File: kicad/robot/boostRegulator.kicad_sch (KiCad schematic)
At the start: 22 parts, among them U5 LSF0102DCTR, U6 MAX77857

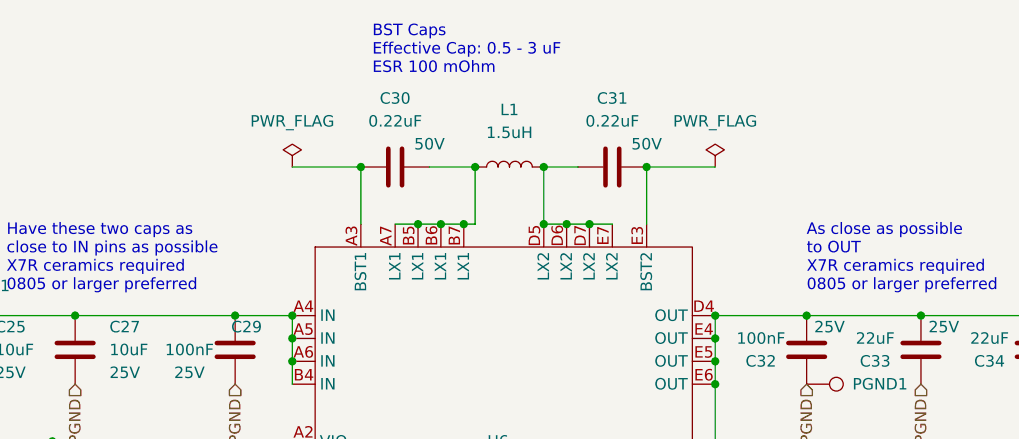
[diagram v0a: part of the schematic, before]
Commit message: Added power flags to Max77857 LX{1,2} pins
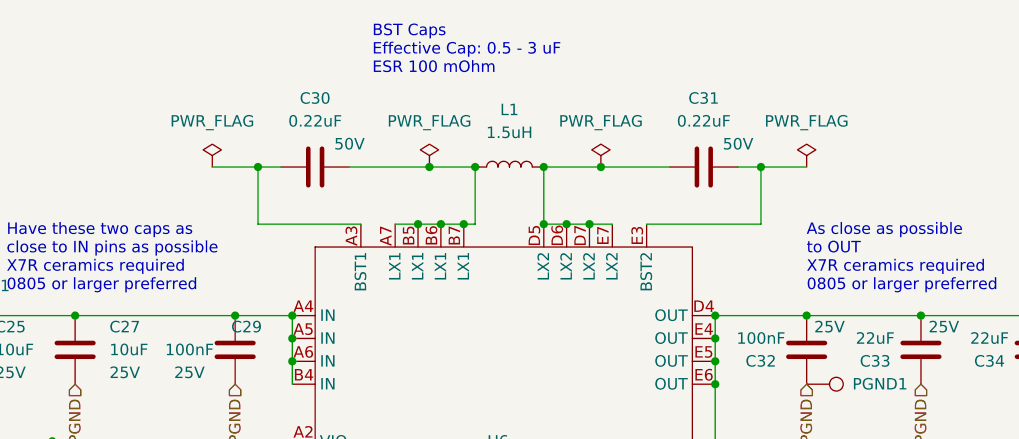
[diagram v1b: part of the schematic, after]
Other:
- moved on the sheet: C30, C31
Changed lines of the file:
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@@
   (junction (at 187.96 80.01) (diameter 0) (color 0 0 0 0)
   )
-  (junction (at 210.82 73.66) (diameter 0) (color 0 0 0 0)
-  )
   (junction (at 189.23 140.97) (diameter 0) (color 0 0 0 0)
   )
@@
   (junction (at 199.39 80.01) (diameter 0) (color 0 0 0 0)
   )
+  (junction (at 205.74 73.66) (diameter 0) (color 0 0 0 0)
+  )
   (junction (at 185.42 80.01) (diameter 0) (color 0 0 0 0)
   )
@@
   (junction (at 118.11 104.14) (diameter 0) (color 0 0 0 0)
   )
+  (junction (at 186.69 73.66) (diameter 0) (color 0 0 0 0)
+  )
   (junction (at 199.39 73.66) (diameter 0) (color 0 0 0 0)
   )
@@
   (junction (at 194.31 140.97) (diameter 0) (color 0 0 0 0)
   )
+  (junction (at 167.64 73.66) (diameter 0) (color 0 0 0 0)
+  )
   (junction (at 228.6 90.17) (diameter 0) (color 0 0 0 0)
   )
-  (junction (at 179.07 73.66) (diameter 0) (color 0 0 0 0)
-  )
   (junction (at 204.47 80.01) (diameter 0) (color 0 0 0 0)
   )
@@
   )
   (junction (at 109.22 129.54) (diameter 0) (color 0 0 0 0)
+  )
+  (junction (at 223.52 73.66) (diameter 0) (color 0 0 0 0)
   )
   (no_connect (at 171.45 121.92))
@@
     (stroke (width 0) (type default) (color 0 0 0 0))
   )
-  (wire (pts (xy 179.07 73.66) (xy 179.07 80.01))
-    (stroke (width 0) (type default) (color 0 0 0 0))
-  )
   (wire (pts (xy 109.22 119.38) (xy 109.22 129.54))
     (stroke (width 0) (type default) (color 0 0 0 0))
@@
     (stroke (width 0) (type default) (color 0 0 0 0))
   )
-  (wire (pts (xy 210.82 73.66) (xy 218.44 73.66))
+  (wire (pts (xy 220.98 73.66) (xy 223.52 73.66))
     (stroke (width 0) (type default) (color 0 0 0 0))
   )
@@
     (stroke (width 0) (type default) (color 0 0 0 0))
   )
+  (wire (pts (xy 210.82 80.01) (xy 223.52 80.01))
+    (stroke (width 0) (type default) (color 0 0 0 0))
+  )
   (wire (pts (xy 194.31 140.97) (xy 196.85 140.97))
     (stroke (width 0) (type default) (color 0 0 0 0))
@@
     (stroke (width 0) (type default) (color 0 0 0 0))
   )
+  (wire (pts (xy 186.69 73.66) (xy 191.77 73.66))
+    (stroke (width 0) (type default) (color 0 0 0 0))
+  )
   (wire (pts (xy 109.22 104.14) (xy 118.11 104.14))
     (stroke (width 0) (type default) (color 0 0 0 0))
@@
     (stroke (width 0) (type default) (color 0 0 0 0))
   )
-  (wire (pts (xy 199.39 73.66) (xy 203.2 73.66))
+  (wire (pts (xy 199.39 73.66) (xy 205.74 73.66))
     (stroke (width 0) (type default) (color 0 0 0 0))
   )
@@
     (stroke (width 0) (type default) (color 0 0 0 0))
   )
+  (wire (pts (xy 223.52 80.01) (xy 223.52 73.66))
+    (stroke (width 0) (type default) (color 0 0 0 0))
+  )
   (wire (pts (xy 109.22 111.76) (xy 109.22 104.14))
     (stroke (width 0) (type default) (color 0 0 0 0))
   )
+  (wire (pts (xy 167.64 80.01) (xy 167.64 73.66))
+    (stroke (width 0) (type default) (color 0 0 0 0))
+  )
   (wire (pts (xy 109.22 129.54) (xy 171.45 129.54))
     (stroke (width 0) (type default) (color 0 0 0 0))
@@
     (stroke (width 0) (type default) (color 0 0 0 0))
   )
-  (wire (pts (xy 186.69 73.66) (xy 191.77 73.66))
-    (stroke (width 0) (type default) (color 0 0 0 0))
-  )
-  (wire (pts (xy 210.82 73.66) (xy 210.82 80.01))
+  (wire (pts (xy 177.8 73.66) (xy 186.69 73.66))
     (stroke (width 0) (type default) (color 0 0 0 0))
   )
@@
     (stroke (width 0) (type default) (color 0 0 0 0))
   )
+  (wire (pts (xy 205.74 73.66) (xy 213.36 73.66))
+    (stroke (width 0) (type default) (color 0 0 0 0))
+  )
   (wire (pts (xy 57.15 116.84) (xy 60.96 116.84))
     (stroke (width 0) (type default) (color 0 0 0 0))
@@
     (stroke (width 0) (type default) (color 0 0 0 0))
   )
+  (wire (pts (xy 223.52 73.66) (xy 228.6 73.66))
+    (stroke (width 0) (type default) (color 0 0 0 0))
+  )
   (wire (pts (xy 254 90.17) (xy 259.08 90.17))
     (stroke (width 0) (type default) (color 0 0 0 0))
@@
     (stroke (width 0) (type default) (color 0 0 0 0))
   )
-  (wire (pts (xy 171.45 73.66) (xy 179.07 73.66))
+  (wire (pts (xy 167.64 73.66) (xy 170.18 73.66))
+    (stroke (width 0) (type default) (color 0 0 0 0))
+  )
+  (wire (pts (xy 162.56 73.66) (xy 167.64 73.66))
     (stroke (width 0) (type default) (color 0 0 0 0))
   )
   (wire (pts (xy 118.11 111.76) (xy 118.11 104.14))
+    (stroke (width 0) (type default) (color 0 0 0 0))
+  )
+  (wire (pts (xy 179.07 80.01) (xy 167.64 80.01))
     (stroke (width 0) (type default) (color 0 0 0 0))
   )
@@
     (effects (font (size 1.27 1.27)) (justify right))
   )
-  (symbol (lib_id "power:PWR_FLAG") (at 218.44 73.66 0) (unit 1)
-    (in_bom yes) (on_board yes) (fields_autoplaced)
-    (property "Reference" "#FLG0104" (id 0) (at 218.44 71.755 0)
-      (effects (font (size 1.27 1.27)) hide)
-    )
-    (property "Value" "PWR_FLAG" (id 1) (at 218.44 68.58 0))
-    (property "Footprint" "" (id 2) (at 218.44 73.66 0)
-      (effects (font (size 1.27 1.27)) hide)
-    )
-    (property "Datasheet" "~" (id 3) (at 218.44 73.66 0)
+  (symbol (lib_id "power:PWR_FLAG") (at 228.6 73.66 0) (unit 1)
+    (in_bom yes) (on_board yes) (fields_autoplaced)
+    (property "Reference" "#FLG0104" (id 0) (at 228.6 71.755 0)
+      (effects (font (size 1.27 1.27)) hide)
+    )
+    (property "Value" "PWR_FLAG" (id 1) (at 228.6 68.58 0))
+    (property "Footprint" "" (id 2) (at 228.6 73.66 0)
+      (effects (font (size 1.27 1.27)) hide)
+    )
+    (property "Datasheet" "~" (id 3) (at 228.6 73.66 0)
       (effects (font (size 1.27 1.27)) hide)
     )
@@
     (pin "2")
   )
+  (symbol (lib_id "power:PWR_FLAG") (at 205.74 73.66 0) (unit 1)
+    (in_bom yes) (on_board yes) (fields_autoplaced)
+    (property "Reference" "#FLG0108" (id 0) (at 205.74 71.755 0)
+      (effects (font (size 1.27 1.27)) hide)
+    )
+    (property "Value" "PWR_FLAG" (id 1) (at 205.74 68.58 0))
+    (property "Footprint" "" (id 2) (at 205.74 73.66 0)
+      (effects (font (size 1.27 1.27)) hide)
+    )
+    (property "Datasheet" "~" (id 3) (at 205.74 73.66 0)
+      (effects (font (size 1.27 1.27)) hide)
+    )
+    (pin "1")
+  )
+  (symbol (lib_id "power:PWR_FLAG") (at 186.69 73.66 0) (unit 1)
+    (in_bom yes) (on_board yes) (fields_autoplaced)
+    (property "Reference" "#FLG0107" (id 0) (at 186.69 71.755 0)
+      (effects (font (size 1.27 1.27)) hide)
+    )
+    (property "Value" "PWR_FLAG" (id 1) (at 186.69 68.58 0))
+    (property "Footprint" "" (id 2) (at 186.69 73.66 0)
+      (effects (font (size 1.27 1.27)) hide)
+    )
+    (property "Datasheet" "~" (id 3) (at 186.69 73.66 0)
+      (effects (font (size 1.27 1.27)) hide)
+    )
+    (pin "1")
+  )
   (symbol (lib_id "Logic_LevelTranslator:LSF0102DCTR") (at 78.74 127 0) (mirror y) (unit 1)
     (in_bom yes) (on_board yes) (fields_autoplaced)
@@
     (pin "2")
   )
-  (symbol (lib_id "power:PWR_FLAG") (at 171.45 73.66 0) (unit 1)
-    (in_bom yes) (on_board yes) (fields_autoplaced)
-    (property "Reference" "#FLG0103" (id 0) (at 171.45 71.755 0)
-      (effects (font (size 1.27 1.27)) hide)
-    )
-    (property "Value" "PWR_FLAG" (id 1) (at 171.45 68.58 0))
-    (property "Footprint" "" (id 2) (at 171.45 73.66 0)
-      (effects (font (size 1.27 1.27)) hide)
-    )
-    (property "Datasheet" "~" (id 3) (at 171.45 73.66 0)
+  (symbol (lib_id "power:PWR_FLAG") (at 162.56 73.66 0) (unit 1)
+    (in_bom yes) (on_board yes) (fields_autoplaced)
+    (property "Reference" "#FLG0103" (id 0) (at 162.56 71.755 0)
+      (effects (font (size 1.27 1.27)) hide)
+    )
+    (property "Value" "PWR_FLAG" (id 1) (at 162.56 68.58 0))
+    (property "Footprint" "" (id 2) (at 162.56 73.66 0)
+      (effects (font (size 1.27 1.27)) hide)
+    )
+    (property "Datasheet" "~" (id 3) (at 162.56 73.66 0)
       (effects (font (size 1.27 1.27)) hide)
     )
@@
     (pin "2")
   )
-  (symbol (lib_id "Device:C") (at 182.88 73.66 90) (unit 1)
-    (in_bom yes) (on_board yes)
-    (property "Reference" "C30" (id 0) (at 182.88 66.04 90))
-    (property "Value" "0.22uF" (id 1) (at 182.88 68.58 90))
-    (property "Footprint" "" (id 2) (at 186.69 72.6948 0)
-      (effects (font (size 1.27 1.27)) hide)
-    )
-    (property "Datasheet" "~" (id 3) (at 182.88 73.66 0)
-      (effects (font (size 1.27 1.27)) hide)
-    )
-    (property "Description" "50V" (id 4) (at 186.69 71.12 90))
+  (symbol (lib_id "Device:C") (at 173.99 73.66 90) (unit 1)
+    (in_bom yes) (on_board yes)
+    (property "Reference" "C30" (id 0) (at 173.99 66.04 90))
+    (property "Value" "0.22uF" (id 1) (at 173.99 68.58 90))
+    (property "Footprint" "" (id 2) (at 177.8 72.6948 0)
+      (effects (font (size 1.27 1.27)) hide)
+    )
+    (property "Datasheet" "~" (id 3) (at 173.99 73.66 0)
+      (effects (font (size 1.27 1.27)) hide)
+    )
+    (property "Description" "50V" (id 4) (at 177.8 71.12 90))
     (pin "1")
     (pin "2")
@@
     (pin "2")
   )
-  (symbol (lib_id "Device:C") (at 207.01 73.66 90) (unit 1)
-    (in_bom yes) (on_board yes)
-    (property "Reference" "C31" (id 0) (at 207.01 66.04 90))
-    (property "Value" "0.22uF" (id 1) (at 207.01 68.58 90))
-    (property "Footprint" "" (id 2) (at 210.82 72.6948 0)
-      (effects (font (size 1.27 1.27)) hide)
-    )
-    (property "Datasheet" "~" (id 3) (at 207.01 73.66 0)
-      (effects (font (size 1.27 1.27)) hide)
-    )
-    (property "Description" "50V" (id 4) (at 210.82 71.12 90))
-    (pin "1")
-    (pin "2")
+  (symbol (lib_id "Device:C") (at 217.17 73.66 90) (unit 1)
+    (in_bom yes) (on_board yes)
+    (property "Reference" "C31" (id 0) (at 217.17 66.04 90))
+    (property "Value" "0.22uF" (id 1) (at 217.17 68.58 90))
+    (property "Footprint" "" (id 2) (at 220.98 72.6948 0)
+      (effects (font (size 1.27 1.27)) hide)
+    )
+    (property "Datasheet" "~" (id 3) (at 217.17 73.66 0)
+      (effects (font (size 1.27 1.27)) hide)
+    )
+    (property "Description" "50V" (id 4) (at 220.98 71.12 90))
+    (pin "1")
+    (pin "2")

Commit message: Updated power input to power output on LX and BST pins for MAX77857 and removed previously assigned power flags
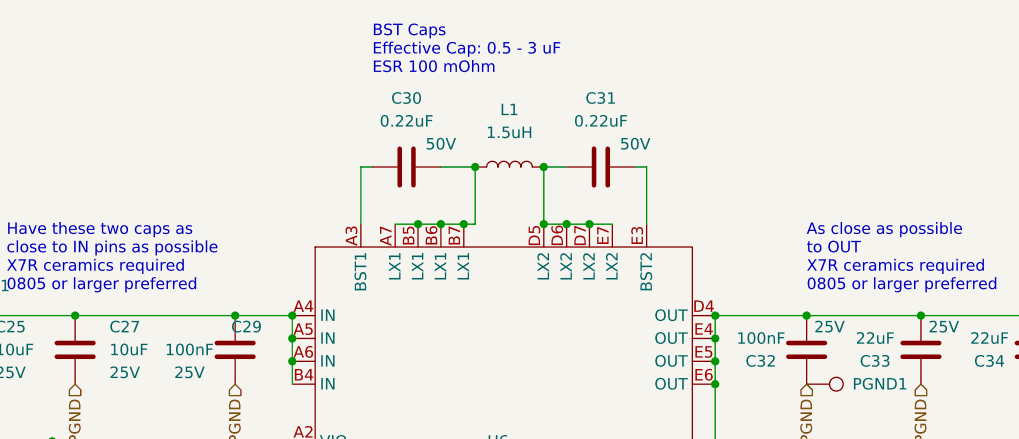
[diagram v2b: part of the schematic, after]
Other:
- moved on the sheet: C30, C31
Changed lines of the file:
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@@
   (junction (at 199.39 80.01) (diameter 0) (color 0 0 0 0)
   )
-  (junction (at 205.74 73.66) (diameter 0) (color 0 0 0 0)
-  )
   (junction (at 185.42 80.01) (diameter 0) (color 0 0 0 0)
   )
@@
   (junction (at 118.11 104.14) (diameter 0) (color 0 0 0 0)
   )
-  (junction (at 186.69 73.66) (diameter 0) (color 0 0 0 0)
-  )
   (junction (at 199.39 73.66) (diameter 0) (color 0 0 0 0)
   )
@@
   (junction (at 194.31 140.97) (diameter 0) (color 0 0 0 0)
   )
-  (junction (at 167.64 73.66) (diameter 0) (color 0 0 0 0)
-  )
   (junction (at 228.6 90.17) (diameter 0) (color 0 0 0 0)
   )
@@
   )
   (junction (at 109.22 129.54) (diameter 0) (color 0 0 0 0)
-  )
-  (junction (at 223.52 73.66) (diameter 0) (color 0 0 0 0)
   )
   (no_connect (at 171.45 121.92))
@@
     (stroke (width 0) (type default) (color 0 0 0 0))
   )
-  (wire (pts (xy 220.98 73.66) (xy 223.52 73.66))
+  (wire (pts (xy 209.55 73.66) (xy 210.82 73.66))
     (stroke (width 0) (type default) (color 0 0 0 0))
   )
@@
     (stroke (width 0) (type default) (color 0 0 0 0))
   )
-  (wire (pts (xy 210.82 80.01) (xy 223.52 80.01))
-    (stroke (width 0) (type default) (color 0 0 0 0))
-  )
   (wire (pts (xy 194.31 140.97) (xy 196.85 140.97))
     (stroke (width 0) (type default) (color 0 0 0 0))
@@
     (stroke (width 0) (type default) (color 0 0 0 0))
   )
-  (wire (pts (xy 186.69 73.66) (xy 191.77 73.66))
+  (wire (pts (xy 187.96 73.66) (xy 191.77 73.66))
     (stroke (width 0) (type default) (color 0 0 0 0))
   )
@@
     (stroke (width 0) (type default) (color 0 0 0 0))
   )
-  (wire (pts (xy 199.39 73.66) (xy 205.74 73.66))
+  (wire (pts (xy 199.39 73.66) (xy 201.93 73.66))
     (stroke (width 0) (type default) (color 0 0 0 0))
   )
@@
     (stroke (width 0) (type default) (color 0 0 0 0))
   )
-  (wire (pts (xy 223.52 80.01) (xy 223.52 73.66))
+  (wire (pts (xy 210.82 80.01) (xy 210.82 73.66))
     (stroke (width 0) (type default) (color 0 0 0 0))
   )
@@
     (stroke (width 0) (type default) (color 0 0 0 0))
   )
-  (wire (pts (xy 167.64 80.01) (xy 167.64 73.66))
+  (wire (pts (xy 179.07 80.01) (xy 179.07 73.66))
     (stroke (width 0) (type default) (color 0 0 0 0))
   )
@@
     (stroke (width 0) (type default) (color 0 0 0 0))
   )
-  (wire (pts (xy 177.8 73.66) (xy 186.69 73.66))
-    (stroke (width 0) (type default) (color 0 0 0 0))
-  )
   (wire (pts (xy 166.37 115.57) (xy 171.45 115.57))
     (stroke (width 0) (type default) (color 0 0 0 0))
@@
     (stroke (width 0) (type default) (color 0 0 0 0))
   )
-  (wire (pts (xy 205.74 73.66) (xy 213.36 73.66))
-    (stroke (width 0) (type default) (color 0 0 0 0))
-  )
   (wire (pts (xy 57.15 116.84) (xy 60.96 116.84))
     (stroke (width 0) (type default) (color 0 0 0 0))
@@
     (stroke (width 0) (type default) (color 0 0 0 0))
   )
-  (wire (pts (xy 223.52 73.66) (xy 228.6 73.66))
-    (stroke (width 0) (type default) (color 0 0 0 0))
-  )
   (wire (pts (xy 254 90.17) (xy 259.08 90.17))
     (stroke (width 0) (type default) (color 0 0 0 0))
@@
     (stroke (width 0) (type default) (color 0 0 0 0))
   )
-  (wire (pts (xy 167.64 73.66) (xy 170.18 73.66))
-    (stroke (width 0) (type default) (color 0 0 0 0))
-  )
-  (wire (pts (xy 162.56 73.66) (xy 167.64 73.66))
+  (wire (pts (xy 179.07 73.66) (xy 180.34 73.66))
     (stroke (width 0) (type default) (color 0 0 0 0))
   )
   (wire (pts (xy 118.11 111.76) (xy 118.11 104.14))
-    (stroke (width 0) (type default) (color 0 0 0 0))
-  )
-  (wire (pts (xy 179.07 80.01) (xy 167.64 80.01))
     (stroke (width 0) (type default) (color 0 0 0 0))
   )
@@
   (hierarchical_label "SCL" (shape input) (at 54.61 127 180)
     (effects (font (size 1.27 1.27)) (justify right))
-  )
-  (symbol (lib_id "power:PWR_FLAG") (at 228.6 73.66 0) (unit 1)
-    (in_bom yes) (on_board yes) (fields_autoplaced)
-    (property "Reference" "#FLG0104" (id 0) (at 228.6 71.755 0)
-      (effects (font (size 1.27 1.27)) hide)
-    )
-    (property "Value" "PWR_FLAG" (id 1) (at 228.6 68.58 0))
-    (property "Footprint" "" (id 2) (at 228.6 73.66 0)
-      (effects (font (size 1.27 1.27)) hide)
-    )
-    (property "Datasheet" "~" (id 3) (at 228.6 73.66 0)
-      (effects (font (size 1.27 1.27)) hide)
-    )
-    (pin "1")
   )
   (symbol (lib_id "Regulator_Switching:MAX77857") (at 194.31 106.68 0) (unit 1)
@@
     (pin "2")
   )
-  (symbol (lib_id "power:PWR_FLAG") (at 205.74 73.66 0) (unit 1)
-    (in_bom yes) (on_board yes) (fields_autoplaced)
-    (property "Reference" "#FLG0108" (id 0) (at 205.74 71.755 0)
-      (effects (font (size 1.27 1.27)) hide)
-    )
-    (property "Value" "PWR_FLAG" (id 1) (at 205.74 68.58 0))
-    (property "Footprint" "" (id 2) (at 205.74 73.66 0)
-      (effects (font (size 1.27 1.27)) hide)
-    )
-    (property "Datasheet" "~" (id 3) (at 205.74 73.66 0)
-      (effects (font (size 1.27 1.27)) hide)
-    )
-    (pin "1")
-  )
-  (symbol (lib_id "power:PWR_FLAG") (at 186.69 73.66 0) (unit 1)
-    (in_bom yes) (on_board yes) (fields_autoplaced)
-    (property "Reference" "#FLG0107" (id 0) (at 186.69 71.755 0)
-      (effects (font (size 1.27 1.27)) hide)
-    )
-    (property "Value" "PWR_FLAG" (id 1) (at 186.69 68.58 0))
-    (property "Footprint" "" (id 2) (at 186.69 73.66 0)
-      (effects (font (size 1.27 1.27)) hide)
-    )
-    (property "Datasheet" "~" (id 3) (at 186.69 73.66 0)
-      (effects (font (size 1.27 1.27)) hide)
-    )
-    (pin "1")
-  )
   (symbol (lib_id "Logic_LevelTranslator:LSF0102DCTR") (at 78.74 127 0) (mirror y) (unit 1)
     (in_bom yes) (on_board yes) (fields_autoplaced)
@@
     (pin "2")
   )
-  (symbol (lib_id "power:PWR_FLAG") (at 162.56 73.66 0) (unit 1)
-    (in_bom yes) (on_board yes) (fields_autoplaced)
-    (property "Reference" "#FLG0103" (id 0) (at 162.56 71.755 0)
-      (effects (font (size 1.27 1.27)) hide)
-    )
-    (property "Value" "PWR_FLAG" (id 1) (at 162.56 68.58 0))
-    (property "Footprint" "" (id 2) (at 162.56 73.66 0)
-      (effects (font (size 1.27 1.27)) hide)
-    )
-    (property "Datasheet" "~" (id 3) (at 162.56 73.66 0)
-      (effects (font (size 1.27 1.27)) hide)
-    )
-    (pin "1")
-  )
   (symbol (lib_id "Device:R") (at 109.22 115.57 0) (unit 1)
     (in_bom yes) (on_board yes)
@@
     (pin "2")
   )
-  (symbol (lib_id "Device:C") (at 173.99 73.66 90) (unit 1)
-    (in_bom yes) (on_board yes)
-    (property "Reference" "C30" (id 0) (at 173.99 66.04 90))
-    (property "Value" "0.22uF" (id 1) (at 173.99 68.58 90))
-    (property "Footprint" "" (id 2) (at 177.8 72.6948 0)
-      (effects (font (size 1.27 1.27)) hide)
-    )
-    (property "Datasheet" "~" (id 3) (at 173.99 73.66 0)
-      (effects (font (size 1.27 1.27)) hide)
-    )
-    (property "Description" "50V" (id 4) (at 177.8 71.12 90))
+  (symbol (lib_id "Device:C") (at 184.15 73.66 90) (unit 1)
+    (in_bom yes) (on_board yes)
+    (property "Reference" "C30" (id 0) (at 184.15 66.04 90))
+    (property "Value" "0.22uF" (id 1) (at 184.15 68.58 90))
+    (property "Footprint" "" (id 2) (at 187.96 72.6948 0)
+      (effects (font (size 1.27 1.27)) hide)
+    )
+    (property "Datasheet" "~" (id 3) (at 184.15 73.66 0)
+      (effects (font (size 1.27 1.27)) hide)
+    )
+    (property "Description" "50V" (id 4) (at 187.96 71.12 90))
     (pin "1")
     (pin "2")
@@
     (pin "2")
   )
-  (symbol (lib_id "Device:C") (at 217.17 73.66 90) (unit 1)
-    (in_bom yes) (on_board yes)
-    (property "Reference" "C31" (id 0) (at 217.17 66.04 90))
-    (property "Value" "0.22uF" (id 1) (at 217.17 68.58 90))
-    (property "Footprint" "" (id 2) (at 220.98 72.6948 0)
-      (effects (font (size 1.27 1.27)) hide)
-    )
-    (property "Datasheet" "~" (id 3) (at 217.17 73.66 0)
-      (effects (font (size 1.27 1.27)) hide)
-    )
-    (property "Description" "50V" (id 4) (at 220.98 71.12 90))
-    (pin "1")
-    (pin "2")
+  (symbol (lib_id "Device:C") (at 205.74 73.66 90) (unit 1)
+    (in_bom yes) (on_board yes)
+    (property "Reference" "C31" (id 0) (at 205.74 66.04 90))
+    (property "Value" "0.22uF" (id 1) (at 205.74 68.58 90))
+    (property "Footprint" "" (id 2) (at 209.55 72.6948 0)
+      (effects (font (size 1.27 1.27)) hide)
+    )
+    (property "Datasheet" "~" (id 3) (at 205.74 73.66 0)
+      (effects (font (size 1.27 1.27)) hide)
+    )
+    (property "Description" "50V" (id 4) (at 209.55 71.12 90))
+    (pin "1")
+    (pin "2")

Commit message: Assigned resistor footprints
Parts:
- R19, R20, R21: footprint (none) -> Resistor_SMD:R_0603_1608Metric
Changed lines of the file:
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@@
       (effects (font (size 1.27 1.27)) (justify left))
     )
-    (property "Footprint" "" (id 2) (at 107.442 115.57 90)
+    (property "Footprint" "Resistor_SMD:R_0603_1608Metric" (id 2) (at 107.442 115.57 90)
       (effects (font (size 1.27 1.27)) hide)
     )
@@
       (effects (font (size 1.27 1.27)) (justify left))
     )
-    (property "Footprint" "" (id 2) (at 55.372 120.65 90)
+    (property "Footprint" "Resistor_SMD:R_0603_1608Metric" (id 2) (at 55.372 120.65 90)
       (effects (font (size 1.27 1.27)) hide)
     )
@@
       (effects (font (size 1.27 1.27)) (justify left))
     )
-    (property "Footprint" "" (id 2) (at 116.332 115.57 90)
-      (effects (font (size 1.27 1.27)) hide)
-    )
+    (property "Footprint" "Resistor_SMD:R_0603_1608Metric" (id 2) (at 116.332 115.57 90)
+      (effects (font (size 1.27 1.27)) hide)
+    )
